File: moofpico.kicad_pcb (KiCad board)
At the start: 4 copper layers, 103.7 x 62.9 mm, 21 parts, among them J1 Serial, J2 Micro_SD_Card, J3 Bus_Apple_II_Card_Side, Q1 BS170, SW2 SW_DIP_x02, U1 Pico, U2 74LVC245, U3 74F11, U4 74LVC245, U5 74LVC245

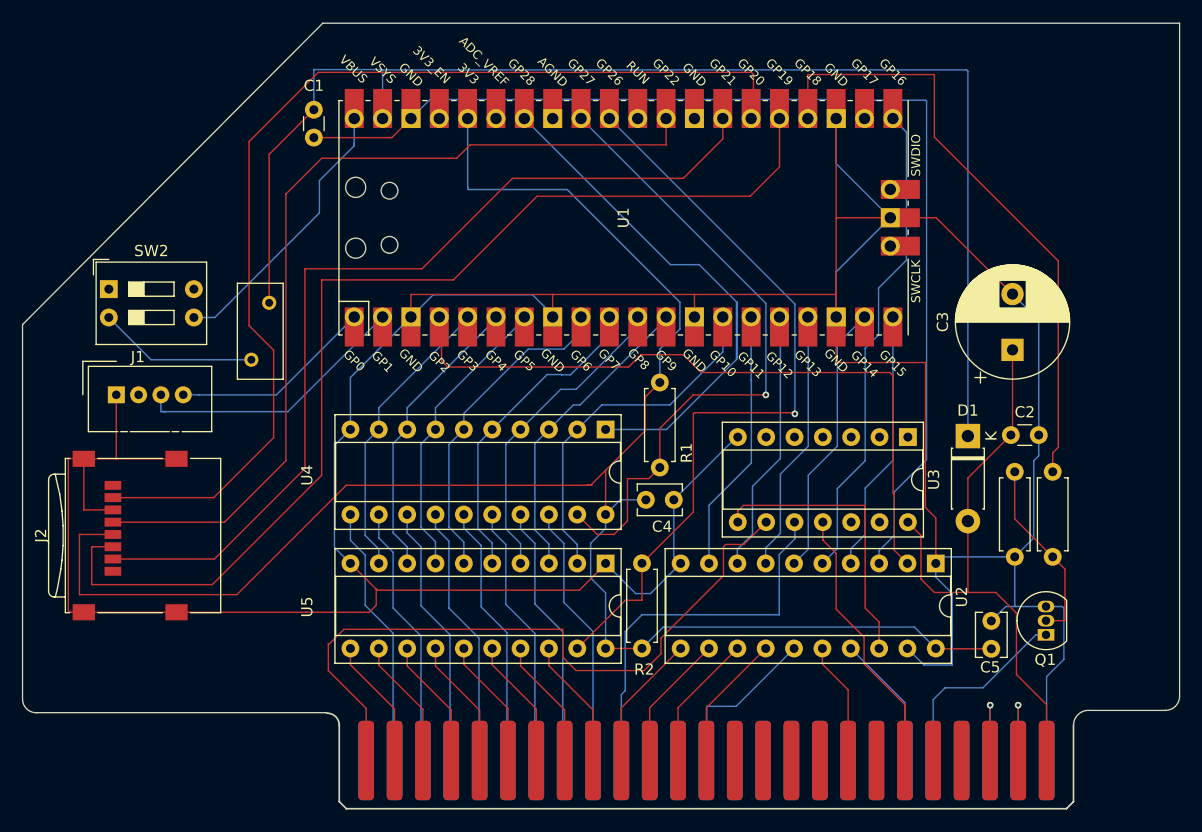
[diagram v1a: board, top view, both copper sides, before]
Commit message: use MEM2061 instead of "generic" SD
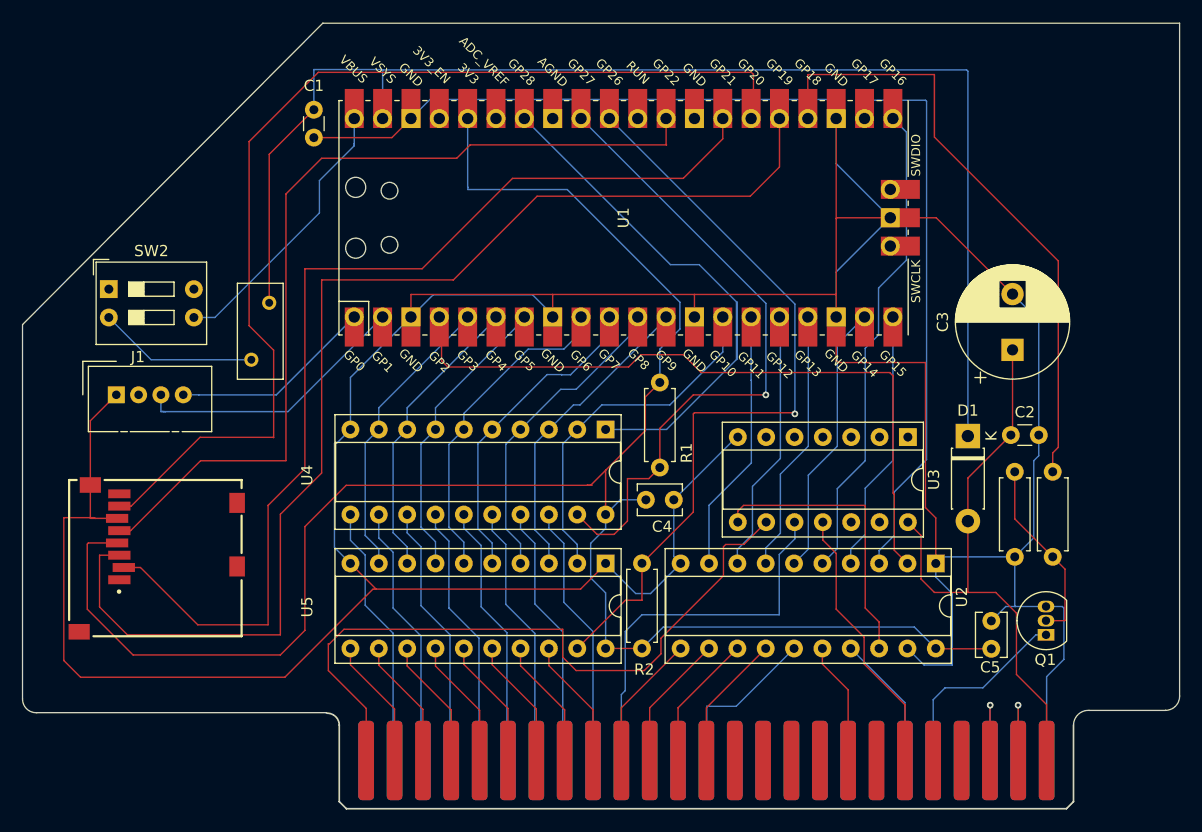
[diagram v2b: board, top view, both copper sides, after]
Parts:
- J2: value Micro_SD_Card -> Micro_SD_Card_Det2; footprint Connector_Card:microSD_HC_Wuerth_693072010801 -> MEM2061_01_188_00_A:GCT_MEM2061-01-188-00-A_REVA
- moved J2 3.03 mm to (97.2, 117.0), turned to -90 degrees
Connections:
- J2 pad 9: GND -> unconnected-(J2-DET_B-Pad9)
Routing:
- net Net-(J2-DAT3/CD): track 82.5 -> 92.4 mm
- net Net-(J2-CMD): track 97.0 -> 106.5 mm
- net +3V3: track 165.3 -> 174.1 mm
- net GND: track 412.7 -> 409.1 mm

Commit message: make +3V3 and GND a little thicker; move +3V3 trace out from between some other RPi traces and onto its own test point/header pin/quasi-via
faffing about with power and ground

but *why*?
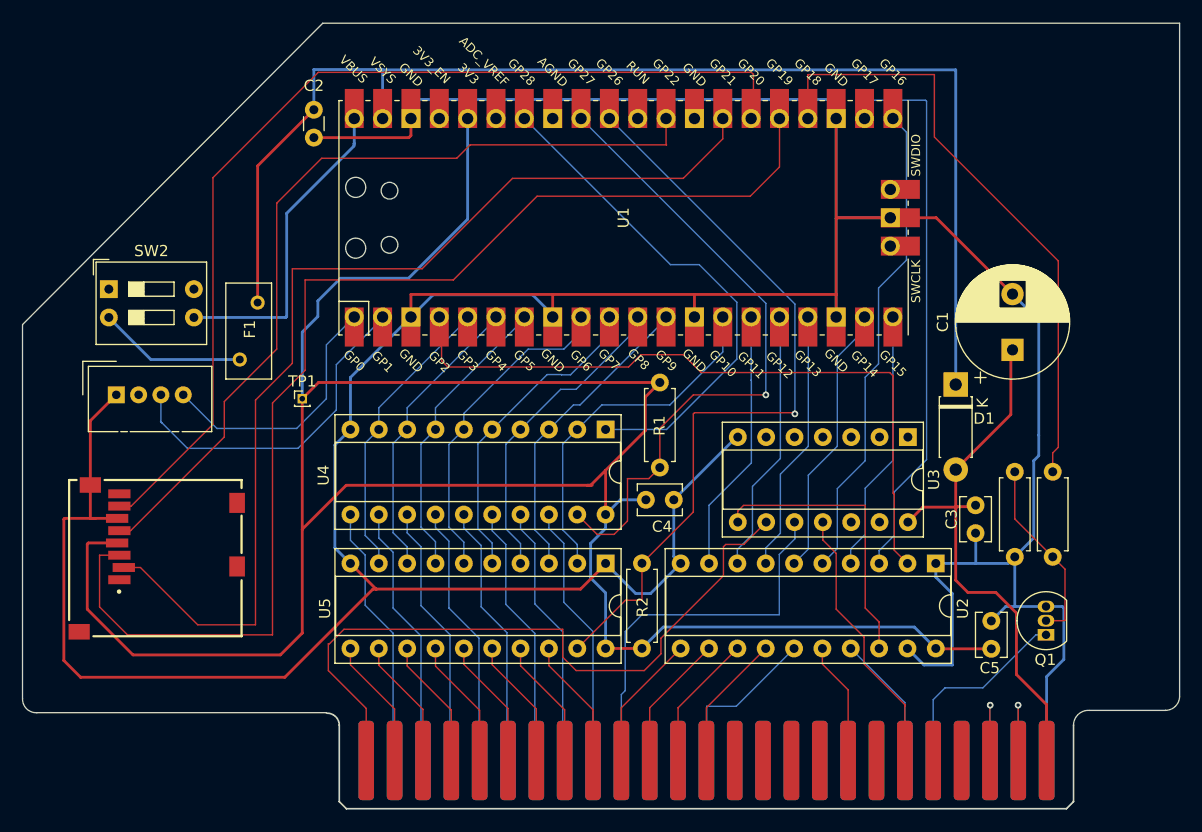
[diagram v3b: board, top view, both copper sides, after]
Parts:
- removed the C2 at (173.8, 106.0)
- added C3: .1u, Capacitor_THT:C_Disc_D3.8mm_W2.6mm_P2.50mm, F.Cu at (170.7, 112.3)
- added TP1: +3V3, Connector_PinHeader_1.00mm:PinHeader_1x01_P1.00mm_Vertical, F.Cu at (110.4, 102.7)
- moved D1 4.74 mm to (168.9, 101.5)
- moved F1 1.04 mm to (104.8, 99.2)
- renumbered C3 to C1, C1 to C2
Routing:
- net +3V3: track 174.1 -> 215.8 mm
- net GND: track 409.1 -> 384.2 mm
- net Net-(J2-DAT0): track 95.6 -> 89.9 mm
- net Net-(J1-Pin_3): track 25.1 -> 30.6 mm
- net Net-(J1-Pin_4): track 18.2 -> 23.5 mm
- net Net-(D1-K): track 118.3 -> 113.1 mm
- net Net-(J2-CLK): track 79.7 -> 75.2 mm
- net Net-(U1-VBUS): track 24.9 -> 28.6 mm
- net +5V: track 52.9 -> 50.3 mm
- net Net-(F1-Pad1): track 14.3 -> 13.3 mm

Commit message: update datasheet URLs; add extra shield pin to uSD
more accurately specify capacitor size

nudged rpi over so that it sat on the mill grid

more footprint futzing

move to 5 pin serial/power connector
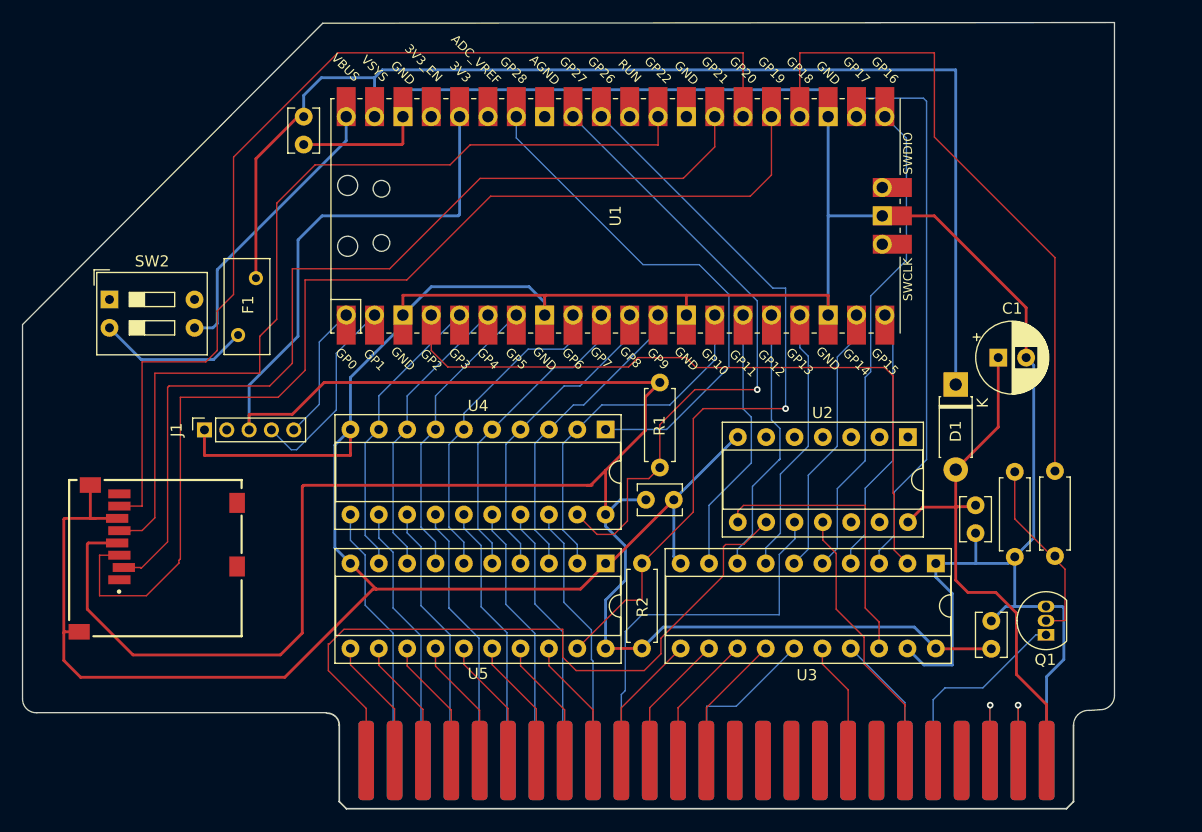
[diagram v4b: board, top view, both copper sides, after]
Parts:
- removed TP1: +3V3, Connector_PinHeader_1.00mm:PinHeader_1x01_P1.00mm_Vertical
- C1: footprint Capacitor_THT:CP_Radial_D10.0mm_P5.00mm -> Capacitor_THT:CP_Radial_D6.3mm_P2.50mm
- C2: value 100nF -> .1u; footprint Capacitor_THT:C_Disc_D3.0mm_W1.6mm_P2.50mm -> Capacitor_THT:C_Disc_D3.8mm_W2.6mm_P2.50mm
- J1: value Serial -> Conn_01x05; footprint Connector:NS-Tech_Grove_1x04_P2mm_Vertical -> Connector_PinSocket_2.00mm:PinSocket_1x05_P2.00mm_Vertical
- moved J1 8.50 mm to (101.6, 105.5)
- moved F1 2.20 mm to (104.6, 97.0)
- moved C1 1.46 mm to (172.7, 99.1), turned to 0 degrees
- moved C2 1.10 mm to (110.5, 77.5)
- moved SW2 0.93 mm to (93.1, 93.9)
- moved U1 0.74 mm to (138.4, 86.4)
- moved R3 0.21 mm to (177.8, 116.8)
- renumbered J3 to J100, U3 to U2, U2 to U3
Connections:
- J1 pad 3: Net-(J1-Pin_3) -> +3V3
- J2 pad 12: (no net) -> GND
- U1 pad 1: Net-(J1-Pin_4) -> Net-(J1-Pin_5)
- U1 pad 2: Net-(J1-Pin_3) -> Net-(J1-Pin_4)
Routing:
- net Net-(J1-Pin_3): track 30.6 -> 0.00 mm
- net Net-(J1-Pin_5): track 0.00 -> 12.2 mm
- net Net-(J2-DAT3/CD): track 92.4 -> 84.4 mm
- net GND: track 384.2 -> 376.4 mm
- net Net-(J2-CMD): track 107.0 -> 99.8 mm
- net +3V3: track 215.8 -> 221.6 mm
- net Net-(J1-Pin_4): track 23.5 -> 17.9 mm
- net Net-(J2-CLK): track 75.2 -> 80.7 mm
- net Net-(J2-DAT0): track 89.9 -> 95.3 mm
- net Net-(D1-K): track 113.1 -> 109.0 mm
- net /3V3‏IRQ: track 55.7 -> 59.7 mm
- net Net-(U1-VBUS): track 28.6 -> 25.5 mm
- net DDIR: track 45.3 -> 46.6 mm
- net +5V: track 50.3 -> 49.3 mm
- net A9: track 23.6 -> 24.3 mm
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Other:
- board size 103.7 x 62.9 mm -> 97.8 x 62.9 mm

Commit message: remove the interior two layers; should have never been there to begin with
notey notey note
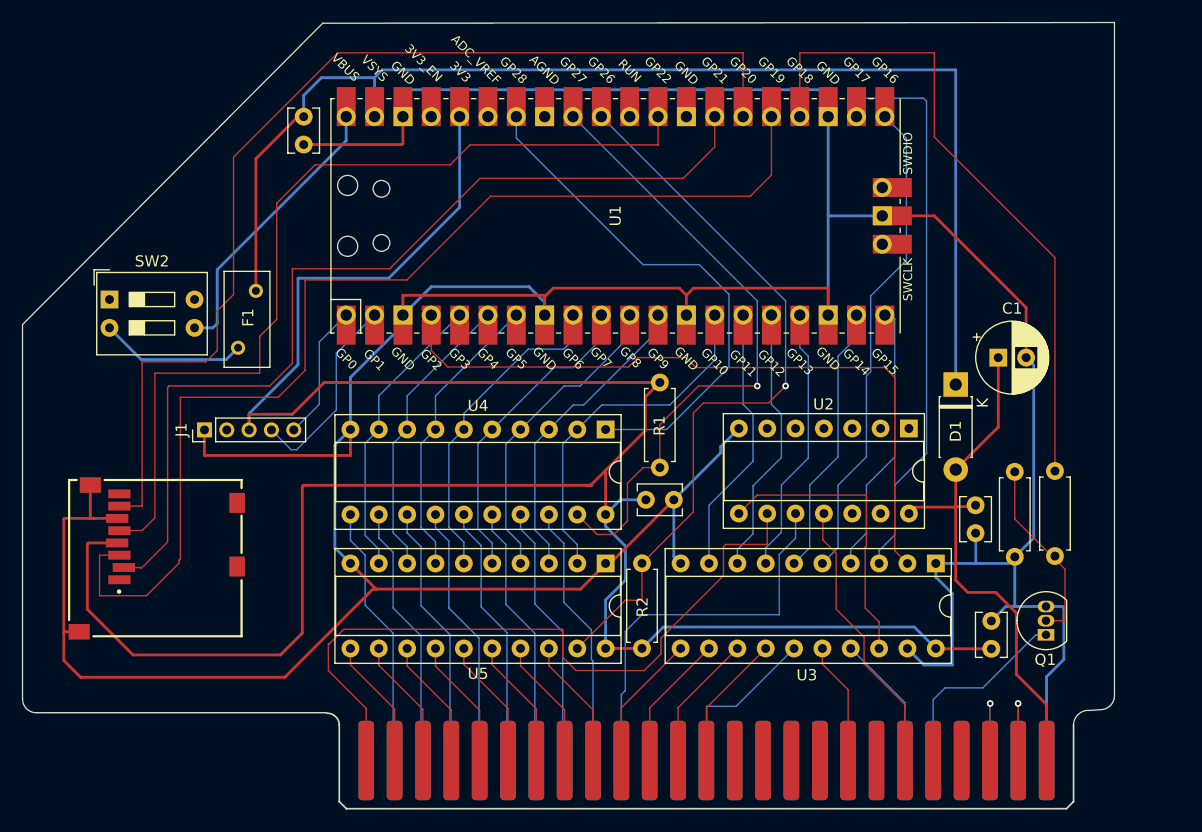
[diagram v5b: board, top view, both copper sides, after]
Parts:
- J1: footprint Connector_PinSocket_2.00mm:PinSocket_1x05_P2.00mm_Vertical -> Connector_PinHeader_2.00mm:PinHeader_1x05_P2.00mm_Vertical
- moved F1 1.14 mm to (104.6, 98.2)
- moved U2 0.78 mm to (164.7, 105.4)
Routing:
- net +3V3: track 221.6 -> 219.2 mm
- net GND: track 376.4 -> 378.6 mm
- net Net-(J100-~{I/O_SELECT}): track 62.5 -> 64.5 mm
- net AL/OE: track 68.1 -> 66.5 mm
- net Net-(D1-K): track 109.0 -> 110.1 mm
- net Net-(J100-~{DEVICE_SELECT}): track 34.8 -> 35.8 mm
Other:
- copper layers 4 -> 2

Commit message: checkpoint: moved the SD card around
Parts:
- J1: value Conn_01x05 -> Conn_01x04; footprint Connector_PinHeader_2.00mm:PinHeader_1x05_P2.00mm_Vertical -> Connector_PinHeader_1.27mm:PinHeader_1x04_P1.27mm_Vertical
- moved J2 85.3 mm to (174.2, 80.4), turned to 180 degrees
- moved R3 25.0 mm to (175.3, 91.9), turned to 180 degrees
- moved SW2 24.8 mm to (106.4, 114.8), turned to 90 degrees
- moved J1 19.5 mm to (109.6, 123.3), turned to 180 degrees
- moved F1 5.08 mm to (105.8, 103.1)
- moved C2 1.29 mm to (109.9, 76.3)
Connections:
- J1 pad 3: +3V3 -> Net-(J1-Pin_3)
- U1 pad 1: Net-(J1-Pin_5) -> Net-(J1-Pin_4)
- U1 pad 2: Net-(J1-Pin_4) -> Net-(J1-Pin_3)
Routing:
- net Net-(J2-CMD): track 99.8 -> 28.0 mm
- net Net-(J2-DAT0): track 95.3 -> 37.9 mm
- net Net-(J2-DAT3/CD): track 84.4 -> 32.5 mm
- net +3V3: track 219.2 -> 188.2 mm
- net Net-(J1-Pin_3): track 0.00 -> 29.3 mm
- net /3V3‏IRQ: track 59.7 -> 31.1 mm
- net Net-(Q1-G): track 16.9 -> 37.1 mm
- net Net-(J2-CLK): track 80.7 -> 64.8 mm
- net Net-(J1-Pin_5): track 12.2 -> 0.00 mm
- net Net-(J1-Pin_4): track 17.9 -> 26.2 mm
- net Net-(D1-K): track 110.1 -> 117.3 mm
- net Net-(U1-VBUS): track 25.5 -> 31.9 mm
- net GND: track 378.6 -> 373.7 mm
- net Net-(F1-Pad1): track 13.1 -> 17.0 mm
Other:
- board size 97.8 x 62.9 mm -> 85.7 x 62.9 mm

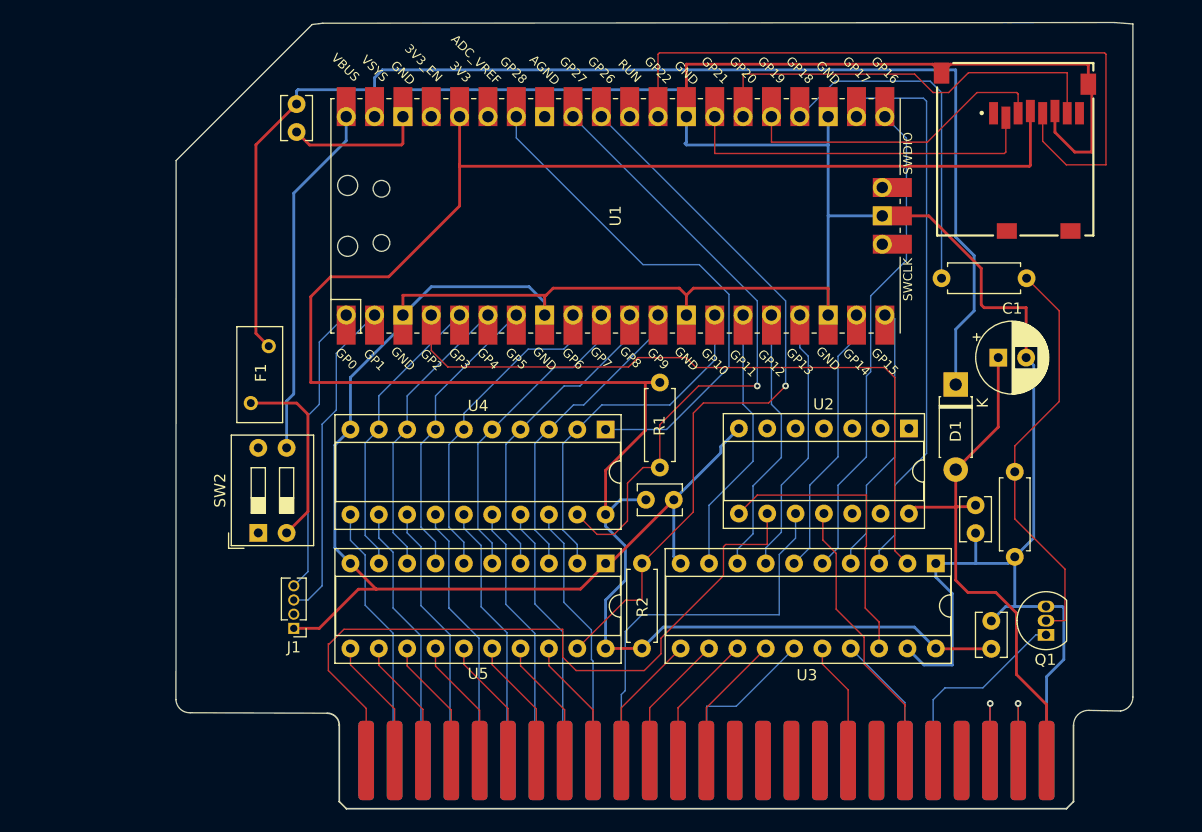
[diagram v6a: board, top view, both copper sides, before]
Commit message: got rid of the vias
don't sneak by that stupid square pin
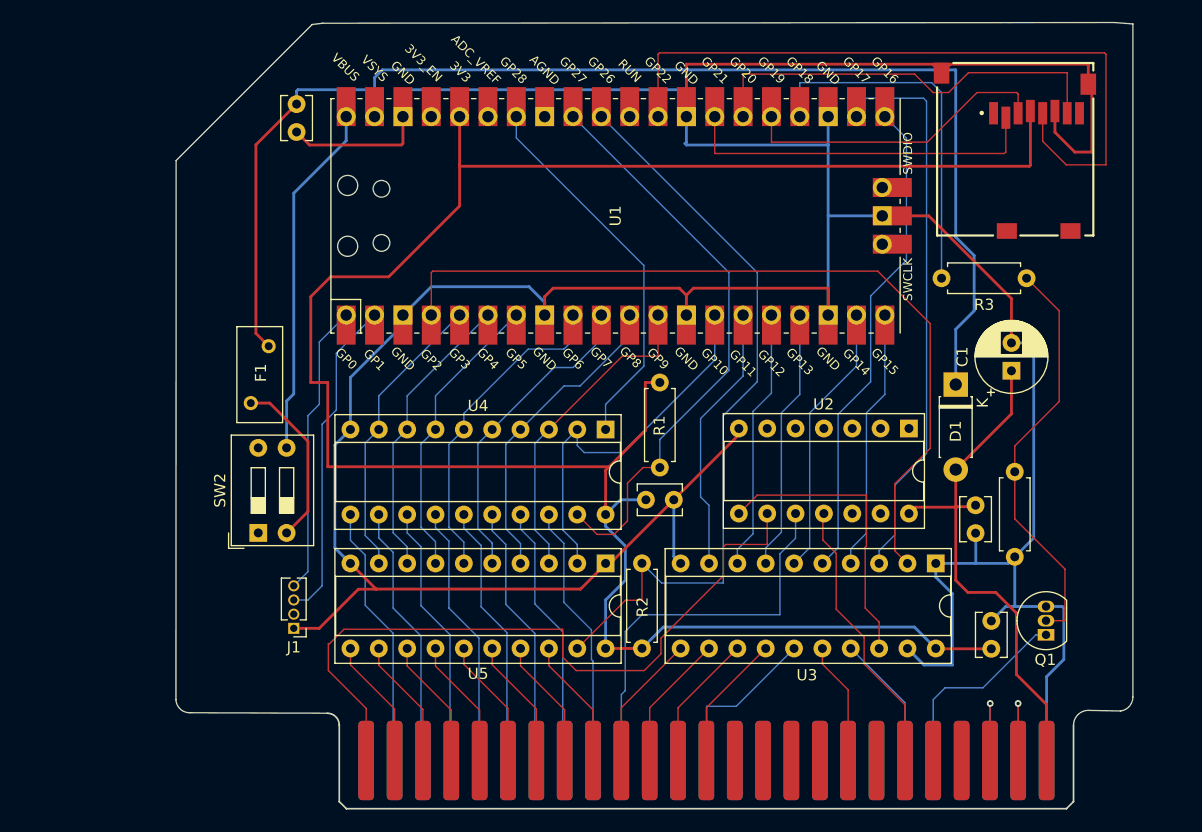
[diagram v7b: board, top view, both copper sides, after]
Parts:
- moved C1 1.67 mm to (173.9, 100.2), turned to 90 degrees
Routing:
- net GND: track 373.7 -> 357.5 mm
- net DDIR: track 46.6 -> 34.2 mm
- net ENBL: track 63.5 -> 73.8 mm
- net D/OE: track 57.6 -> 52.4 mm, vias 1 -> 0
- net +3V3: track 188.2 -> 191.2 mm
- net AD7: track 32.0 -> 34.6 mm
- net /3V3‏IRQ: track 31.1 -> 32.8 mm
- net Net-(F1-Pad1): track 17.0 -> 15.5 mm
- net AD6: track 27.9 -> 29.2 mm
- net AL/OE: track 66.5 -> 67.7 mm, vias 1 -> 0
- net A9: track 24.3 -> 23.5 mm
- net +5V: track 48.8 -> 48.2 mm
- net A10: track 24.1 -> 23.5 mm
